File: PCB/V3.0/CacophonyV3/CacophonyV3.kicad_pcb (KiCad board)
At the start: 2 copper layers, 61.1 x 47 mm, 28 parts, among them J1 Conn_01x04, J2 Conn_01x05, J3 Conn_01x03, J4 Conn_01x03, J5 Conn_01x03, J6 Conn_01x02

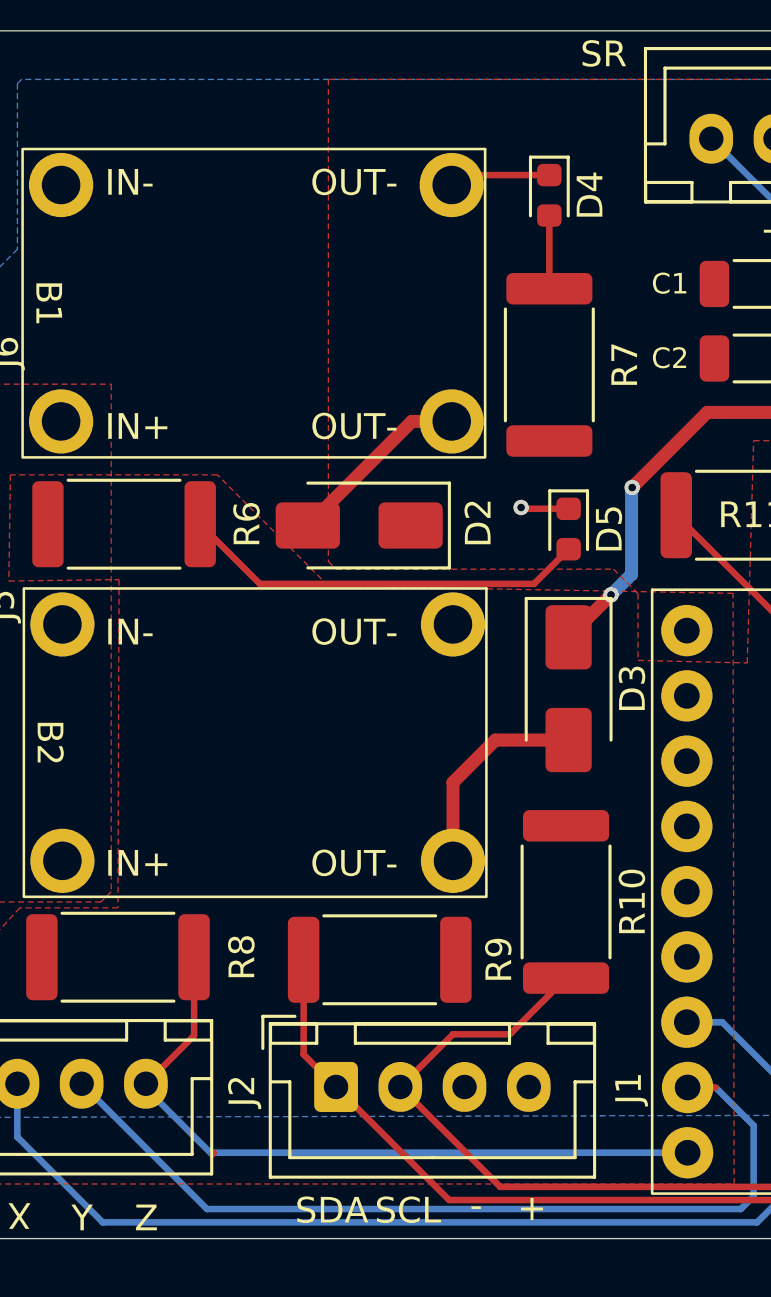
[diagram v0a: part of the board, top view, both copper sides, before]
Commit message: Fixed OLED Display
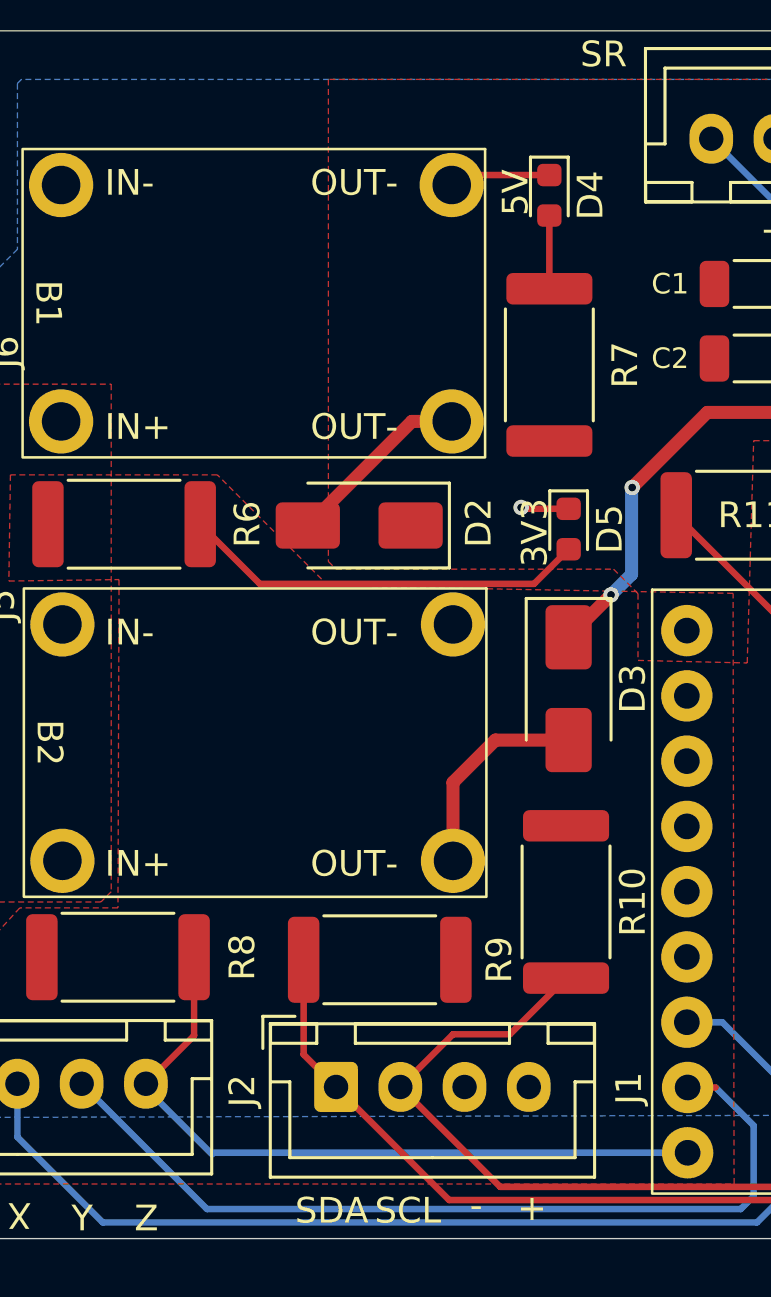
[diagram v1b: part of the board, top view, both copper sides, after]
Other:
- board text added: "3V3"
- board text added: "5V"
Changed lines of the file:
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@@
+		)
+	)
+	(gr_text "5V"
+		(at 144.57 59.2 90)
+		(layer "F.SilkS")
+		(effects
+			(font
+				(size 1 1)
+				(thickness 0.1)
+			)
+			(justify left bottom)
 		)
 	)
@@
 	(gr_text "X"
 		(at 125.15 97.5 180)
+		(layer "F.SilkS")
+		(effects
+			(font
+				(size 1 1)
+				(thickness 0.1)
+			)
+			(justify left bottom)
+		)
+	)
+	(gr_text "3V3"
+		(at 145.315 72.8675 90)
 		(layer "F.SilkS")
 		(effects
@@
 		(width 0.254)
 		(layer "F.Cu")
-		(net 20)
-	)
-	(segment
-		(start 132.175 95.725)
-		(end 132.24 95.66)
-		(width 0.254)
-		(layer "F.Cu")

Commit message: New PCB
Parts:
- added R101: 200k, Resistor_SMD:R_0402_1005Metric, F.Cu at (75.3, 80.0)
- added R102: 100k, Resistor_SMD:R_0402_1005Metric, F.Cu at (77.4, 80.0)
- added REF**: MountingHole_3.2mm_M3, MountingHole:MountingHole_3.2mm_M3, F.Cu at (42.1, 63.0)
- C1, C2, C3, C4: footprint Capacitor_SMD:C_1206_3216Metric -> Resistor_SMD:R_0402_1005Metric
- D4, D5: footprint LED_SMD:LED_0603_1608Metric -> LED_SMD:LED_0402_1005Metric
- R10, R11, R12, R6, R8, R9: footprint Resistor_SMD:R_2512_6332Metric -> Resistor_SMD:R_0402_1005Metric
- R7: footprint Resistor_SMD:R_2512_6332Metric -> Capacitor_SMD:C_0402_1005Metric
- moved REF** 131.1 mm to (42.0, 100.0)
- moved J4 125.0 mm to (50.2, 97.9), turned to 0 degrees
- moved C3 116.3 mm to (51.3, 92.6), turned to 180 degrees
- moved C4 115.1 mm to (51.3, 90.7), turned to 180 degrees
- moved J3 102.4 mm to (63.1, 97.9), turned to 0 degrees
- moved C1 87.8 mm to (73.5, 98.6), turned to 180 degrees
- moved C2 87.1 mm to (73.5, 99.9), turned to 180 degrees
- moved D4 79.7 mm to (77.2, 99.9), turned to 0 degrees
- moved R7 75.9 mm to (77.2, 98.6), turned to 0 degrees
- moved B1 73.7 mm to (55.7, 86.8)
- moved IC1 73.4 mm to (103.5, 67.7)
- moved U1 71.3 mm to (88.0, 85.4)
- moved D3 70.3 mm to (75.8, 75.4)
- moved D5 70.0 mm to (76.1, 69.0), turned to 0 degrees
- moved B2 70.0 mm to (55.7, 73.0)
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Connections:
- IC1 pad 2: +3.3V -> +5V
- U1 pad 13: /PWM_R -> /PWM_L
- U1 pad 14: /PWM_L -> /PWM_R
- U1 pad 5: unconnected-(U1-IO2-Pad5) -> /VOut
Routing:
- net +5V: track 0.00 -> 80.3 mm, vias 0 -> 2
- net /PWM_L: track 32.4 -> 80.8 mm
- net +3.3V: track 36.8 -> 0.00 mm, vias 2 -> 0
- net /SDA: track 38.0 -> 15.6 mm
- net /PWM_R: track 40.3 -> 62.3 mm
- net Net-(IC1-TX): track 21.7 -> 2.55 mm
- net +9V: track 0.00 -> 19.1 mm
- net /JOYX: track 42.5 -> 23.8 mm
- net /SCL: track 38.9 -> 23.1 mm
- net Net-(D5-A): track 15.9 -> 1.31 mm
- net /JOYY: track 34.3 -> 20.2 mm
- net /ESP_Tx: track 8.25 -> 20.0 mm
- net GND: track 12.7 -> 23.8 mm, vias 5 -> 0
- net /VOut: track 0.00 -> 10.1 mm
- net /ESP_Rx: track 18.6 -> 8.69 mm
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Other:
- board size 61.1 x 47 mm -> 79 x 46 mm
- board text added: "OUT+"

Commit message: PCBv3 Fabrication
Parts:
- added G***: LOGO, Decals:Axolotl, B.Cu at (40.7, 89.9)
- moved REF** 0.10 mm to (42.0, 63.0)
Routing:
- net +BATT: track 0.00 -> 8.11 mm
- net GND: track 23.8 -> 24.8 mm, vias 0 -> 1
- net /PWM_L: vias 0 -> 1
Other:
- board size 79 x 46 mm -> 76 x 45 mm
- board text added: "Made by: Ryusei Kinosaki"

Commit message: SImplified UI, fixed JS
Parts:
- R11, R12: value 10k -> 1k
- moved IC1 2.10 mm to (103.5, 65.6)
- moved R12 1.80 mm to (105.2, 74.2)
- moved R11 1.69 mm to (100.1, 71.7)
- moved J4 0.20 mm to (50.0, 97.9)
- moved J3 0.10 mm to (63.0, 97.9)
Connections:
- J1 pad 1: /SDA -> +3.3V
- J1 pad 2: /SCL -> GND
- J1 pad 3: GND -> /SCL
- J1 pad 4: +3.3V -> /SDA
- J2 pad 1: GND -> /JOYSW
- J2 pad 2: +3.3V -> /JOYY
- J2 pad 4: /JOYY -> +3.3V
- J2 pad 5: /JOYSW -> GND
- J3 pad 1: GND -> /PWM_R
- J3 pad 3: /PWM_R -> GND
- J4 pad 1: GND -> /PWM_L
- J4 pad 3: /PWM_L -> GND
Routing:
- net /JOYY: track 20.2 -> 33.3 mm
- net /JOYX: track 23.8 -> 33.2 mm
- net /PWM_R: track 62.3 -> 68.9 mm
- net /SDA: track 15.6 -> 21.6 mm, vias 0 -> 1
- net /PWM_L: track 80.8 -> 85.1 mm, vias 1 -> 0
- net GND: track 24.8 -> 20.4 mm, vias 1 -> 2
- net /SCL: track 23.1 -> 26.5 mm
- net /JOYSW: track 33.9 -> 36.6 mm
- net /ESP_Rx: track 8.69 -> 7.00 mm
- net /ESP_Tx: track 20.0 -> 21.3 mm
